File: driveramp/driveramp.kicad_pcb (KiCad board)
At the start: 2 copper layers, 109 x 79 mm, 86 parts, among them J1 SMA, J2 SMA, K1 CONN_3, K2 CONN_3, P2 CONN_2, Q1 BC547BTA, T1 MABACT0067, T2 2x Fair-Rite 2843006802, coax, U1 ISL43210A, U2 MRFE6VP100H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

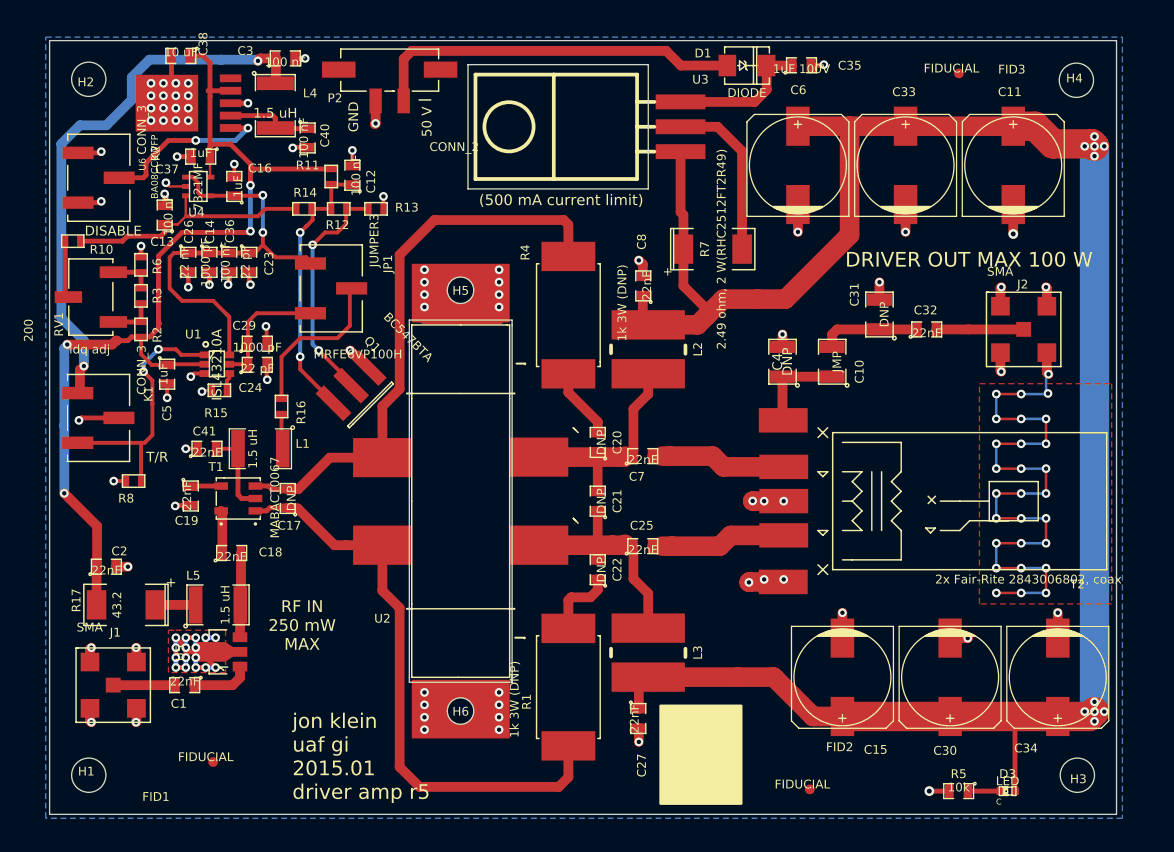
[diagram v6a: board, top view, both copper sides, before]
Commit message: cleaned up silkscreen, moved fiduciary marks at least 4.75ish mm away from board edges
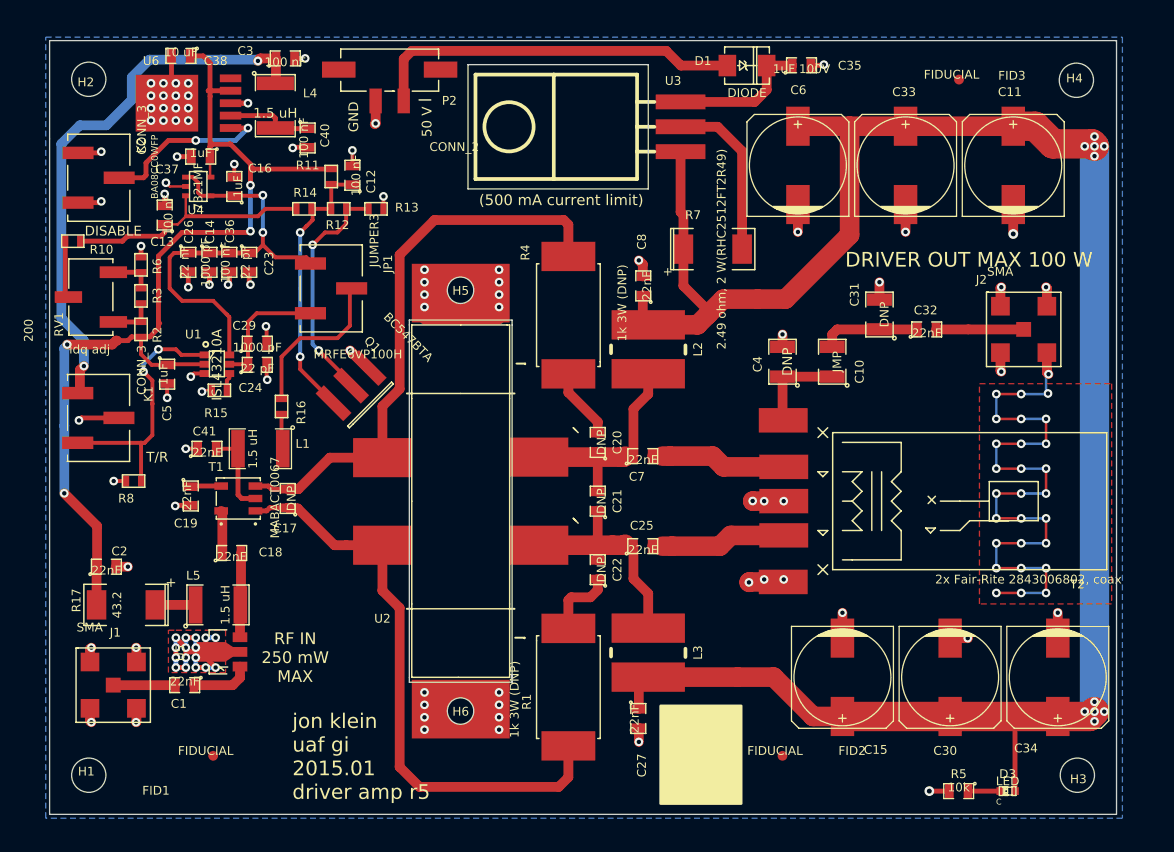
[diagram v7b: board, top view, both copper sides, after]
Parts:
- moved FID2 4.42 mm to (150.9, 136.0)
- moved FID1 0.63 mm to (92.7, 136.0)
- moved FID3 0.63 mm to (168.9, 66.9)
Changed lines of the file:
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@@
     (links 149)
     (no_connects 0)
-    (area 75.949999 62.899999 185.050001 142.050001)
+    (area 72.285786 62.6 187.328215 143.92376)
     (thickness 1.6)
     (drawings 40)
@@
   )
   (setup
-    (last_trace_width 0.5)
+    (last_trace_width 0.254)
     (user_trace_width 0.4)
     (user_trace_width 0.5)
@@
     (pad_to_paste_clearance -0.05)
     (aux_axis_origin 0 0)
+    (grid_origin 143.637 75.438)
     (visible_elements FFFEFF7F)
     (pcbplotparams
-      (layerselection 284196865)
+      (layerselection 284721153)
       (usegerberextensions true)
       (excludeedgelayer true)
@@
     (descr "TO-220, Neutral, Horizontal,")
     (tags "TO-220, Neutral, Horizontal,")
-    (fp_text reference U3 (at 4.826 2.794 180) (layer F.SilkS)
+    (fp_text reference U3 (at 4.699 0 180) (layer F.SilkS)
       (effects (font (size 0.9 0.9) (thickness 0.225)))
     )
@@
   (module local:2-1445053-2 (layer F.Cu)
     (at 110.744 65.913 180)
-    (fp_text reference P2 (at 5.588 -2.921 180) (layer F.SilkS)
+    (fp_text reference P2 (at -6.096 -3.175 180) (layer F.SilkS)
       (effects (font (size 0.9 0.9) (thickness 0.225)))
     )
@@
     (tags "CMS SM")
     (attr smd)
-    (fp_text reference R7 (at -0.8001 0 90) (layer F.SilkS)
+    (fp_text reference R7 (at -2.018 -3.478 180) (layer F.SilkS)
       (effects (font (size 0.9 0.9) (thickness 0.225)))
     )
@@
   (module local:SMA_0732511350 (layer F.Cu)
     (at 175.514 92.456)
-    (fp_text reference J2 (at -0.1 -4.6) (layer F.SilkS)
+    (fp_text reference J2 (at -4.318 -5.08) (layer F.SilkS)
       (effects (font (size 0.9 0.9) (thickness 0.225)))
     )
@@
     (at 91.186 77.851 270)
     (attr smd)
-    (fp_text reference U4 (at 2.649 0.186 360) (layer F.SilkS)
+    (fp_text reference U4 (at 2.413 0.254 360) (layer F.SilkS)
       (effects (font (size 0.9 0.9) (thickness 0.225)))
     )
@@
     (at 89.408 64.516 180)
     (attr smd)
-    (fp_text reference C38 (at -2.294 1.225 270) (layer F.SilkS)
+    (fp_text reference C38 (at -3.556 -0.508 360) (layer F.SilkS)
       (effects (font (size 0.9 0.9) (thickness 0.225)))
     )
@@
     (at 100.33 109.728 90)
     (attr smd)
-    (fp_text reference C17 (at -2.772 0.17 180) (layer F.SilkS)
+    (fp_text reference C17 (at -3.048 -0.254 180) (layer F.SilkS)
       (effects (font (size 0.9 0.9) (thickness 0.225)))
     )
@@
     (at 90.424 109.474 270)
     (attr smd)
-    (fp_text reference C19 (at 2.526 0.424 360) (layer F.SilkS)
+    (fp_text reference C19 (at 2.794 0.508 360) (layer F.SilkS)
       (effects (font (size 0.9 0.9) (thickness 0.225)))
     )
@@
     (tags "DO-214AA SMB")
     (attr smd)
-    (fp_text reference D1 (at -4.5 -1.25) (layer F.SilkS)
+    (fp_text reference D1 (at -4.502 -0.476) (layer F.SilkS)
       (effects (font (size 0.9 0.9) (thickness 0.225)))
     )
@@
   )
   (module sdtransmitter:FID_1MM (layer F.Cu)
-    (at 92.71 136.652)
+    (at 92.71 136.017)
     (fp_text reference FID1 (at -5.842 3.556) (layer F.SilkS)
       (effects (font (size 0.9 0.9) (thickness 0.225)))
@@
   )
   (module sdtransmitter:FID_1MM (layer F.Cu)
-    (at 153.67 139.446)
-    (fp_text reference FID2 (at 3.048 -4.318) (layer F.SilkS)
+    (at 150.876 136.017)
+    (fp_text reference FID2 (at 7.112 -0.508) (layer F.SilkS)
       (effects (font (size 0.9 0.9) (thickness 0.225)))
     )
@@
   )
   (module sdtransmitter:FID_1MM (layer F.Cu)
-    (at 168.9 66.3)
+    (at 168.91 66.929)
     (fp_text reference FID3 (at 5.4 -0.4) (layer F.SilkS)
       (effects (font (size 0.9 0.9) (thickness 0.225)))
@@
     (tags "CMS SM")
     (attr smd)
-    (fp_text reference C4 (at 0 -0.508 90) (layer F.SilkS)
-      (effects (font (size 1 1) (thickness 0.15)))
+    (fp_text reference C4 (at -0.254 -2.54 90) (layer F.SilkS)
+      (effects (font (size 0.9 0.9) (thickness 0.225)))
     )
     (fp_text value DNP (at 0 0.508 90) (layer F.SilkS)
@@
   (module sdtransmitter:0740991003 (layer F.Cu)
     (at 81.026 76.962 270)
-    (fp_text reference K2 (at -2.5 -5.8 270) (layer F.SilkS)
+    (fp_text reference K2 (at -3.302 -4.318 270) (layer F.SilkS)
       (effects (font (size 0.9 0.9) (thickness 0.225)))
     )
@@
   (module to252_5:TO252-5 (layer F.Cu)
     (at 94.488 69.342 90)
-    (fp_text reference U6 (at -6.25 -9 90) (layer F.SilkS)
-      (effects (font (size 0.7 0.7) (thickness 0.175)))
+    (fp_text reference U6 (at 4.318 -8.128 180) (layer F.SilkS)
+      (effects (font (size 0.9 0.9) (thickness 0.225)))
     )
     (fp_text value BA08CC0WFP (at -6.5 -7.75 90) (layer F.SilkS)
@@
   (gr_line (start 118.745 78.105) (end 137.16 78.105) (angle 90) (layer Edge.Cuts) (width 0.1))
   (gr_line (start 118.745 65.405) (end 118.745 78.105) (angle 90) (layer Edge.Cuts) (width 0.1))
-  (gr_text "RF IN\n250 mW\nMAX" (at 101.8 122.7) (layer F.SilkS)
+  (gr_text "RF IN\n250 mW\nMAX" (at 101.092 125.984) (layer F.SilkS)
     (effects (font (size 1.2 1.2) (thickness 0.3)))
   )
@@
     (effects (font (size 1.5 1.5) (thickness 0.3)) (justify left))
   )
-  (segment (start 78.899 79.502) (end 81.153 79.502) (width 0.5) (layer F.Cu) (net 1) (status 400000))
+  (segment (start 78.899 79.502) (end 81.153 79.502) (width 0.5) (layer F.Cu) (net 1))
   (via (at 81.28 79.375) (size 0.889) (layers F.Cu B.Cu) (net 1))
   (segment (start 81.153 79.502) (end 81.28 79.375) (width 0.5) (layer F.Cu) (net 1))
-  (segment (start 78.899 74.422) (end 81.153 74.422) (width 0.5) (layer F.Cu) (net 1) (status 400000))
+  (segment (start 78.899 74.422) (end 81.153 74.422) (width 0.5) (layer F.Cu) (net 1))
   (via (at 81.28 74.295) (size 0.889) (layers F.Cu B.Cu) (net 1))
   (segment (start 81.153 74.422) (end 81.28 74.295) (width 0.5) (layer F.Cu) (net 1))

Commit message: DFM changes..
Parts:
- added R9: 1.1k 1%, SMD_Packages:SMD-0603, F.Cu at (79.4, 82.7)
- C1, C18, C19, C2, C25, C27, C32, C41, C7, C8: value 22nF -> 22 nF
- C10: value JMP -> 22 nF; footprint SMD_Packages:SMD-1210 -> SMD_Packages:SMD-0805
- JP1: value JUMPER3 -> SMD_HDR
- K1, K2: value CONN_3 -> SMD_HDR
- R10: value 2k 1% -> 909 1%
- moved R10 4.13 mm to (82.4, 82.7), turned to 0 degrees
- moved C10 3.39 mm to (156.7, 92.5), turned to 0 degrees
- moved FID3 1.53 mm to (169.0, 68.5)
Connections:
- R10 pad 1: Net-(C13-Pad1) -> Net-(R10-Pad1)
- R10 pad 2: Net-(R10-Pad2) -> Net-(C13-Pad1)
- RV1 pad 2: Net-(R10-Pad2) -> Net-(R9-Pad1)
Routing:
- net Net-(R9-Pad1): track 0.00 -> 7.41 mm
- net Net-(R10-Pad2): track 5.85 -> 0.00 mm
- net Net-(C13-Pad1): track 26.0 -> 21.2 mm
- net Net-(C10-Pad1): track 9.75 -> 13.2 mm
- net Net-(C10-Pad2): track 10.2 -> 6.98 mm
- net Net-(R10-Pad1): track 0.00 -> 1.52 mm
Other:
- board size 109 x 79 mm -> 108.7 x 79.2 mm
